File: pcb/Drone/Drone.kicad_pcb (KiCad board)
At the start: 2 copper layers, 72 x 72 mm, 61 parts, among them J1 USB_C_Receptacle_USB2.0_16P, J10 JST1.25, J2 JST1.25, J3 JST1.25, J4 JST1.25, J5 JST1.25, J6 JST1.25, J7 JST1.25, J8 JST1.25, J9 JST1.25, Q1 SS8050, Q2 SS8050, Q3 Si2301, SW1 RST, SW2 BOOT, U1 esp32s3_wroom1, U10 AP2112K-3.3, U2 DW01A, U4 USBLC6-2SC6, U5 8205, U6 CP2102, U8 ME6211C33M5, U9 ME6211C33M5

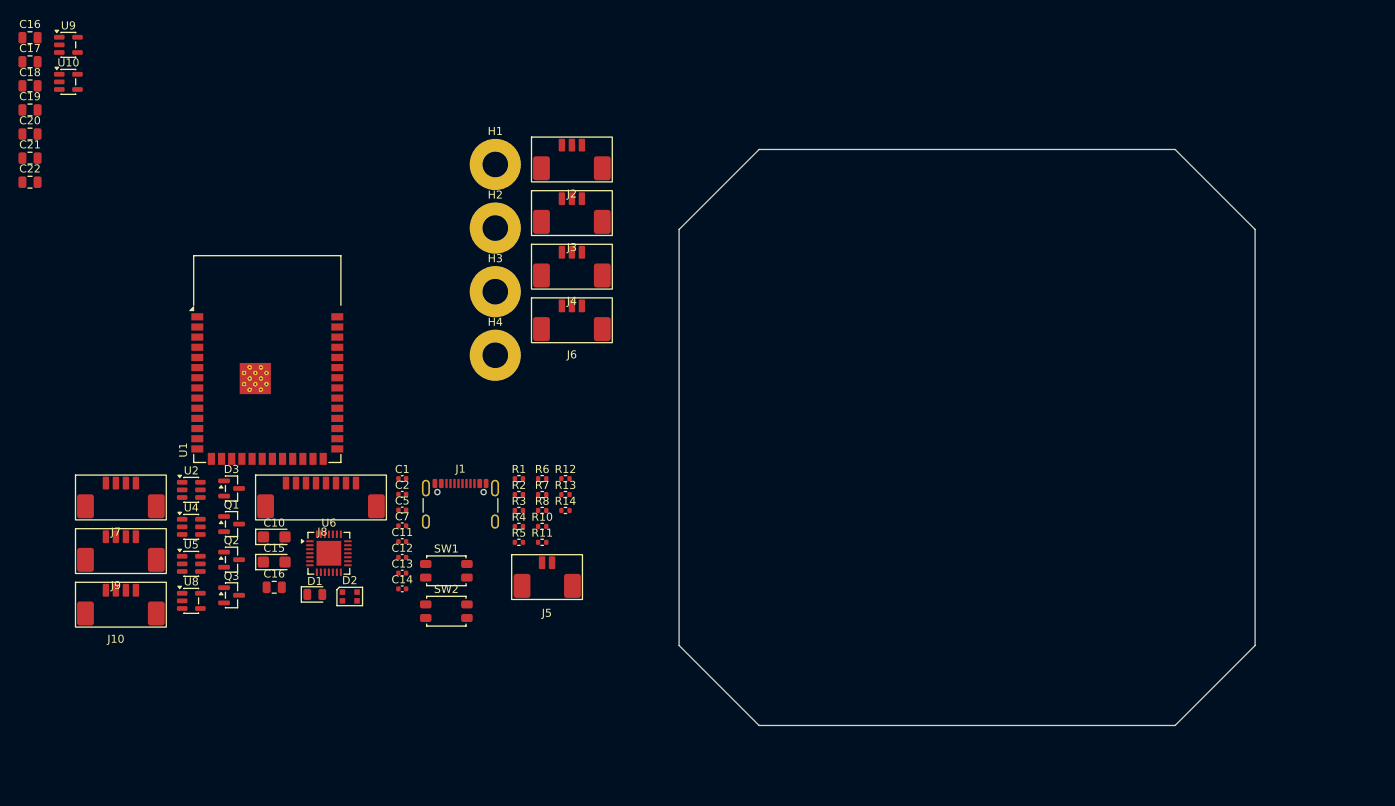
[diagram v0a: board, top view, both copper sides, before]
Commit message: pcb layout: complete component positions
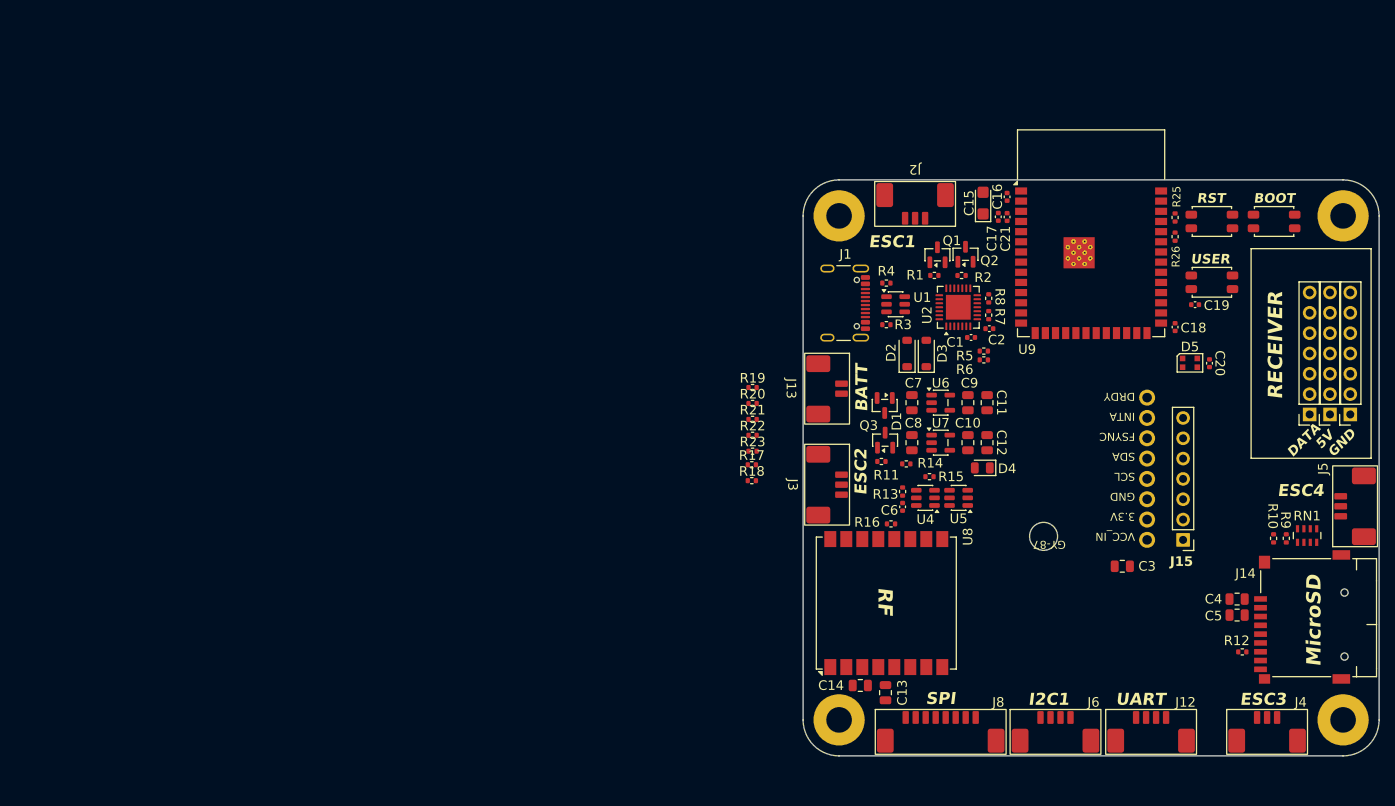
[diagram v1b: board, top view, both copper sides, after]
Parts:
- removed the C16 at (71.6, 113.2)
- removed the C16 at (41.1, 44.5)
- removed C22: 0.1u, Capacitor_SMD:C_0805_2012Metric
- removed J7: JST1.25, JST_1.25mm_RA_SMD:JST_1.25mm_RA_SMD_4P
- removed U10: AP2112K-3.3, Package_TO_SOT_SMD:SOT-23-5
- added C16: 0.1u, Capacitor_SMD:C_0402_1005Metric, F.Cu at (163.2, 64.4)
- added C3: 0.1u, Capacitor_SMD:C_0805_2012Metric, F.Cu at (177.6, 110.6)
- added C4: 10u, Capacitor_SMD:C_0805_2012Metric, F.Cu at (192.0, 114.7)
- added C6: 0.1u, Capacitor_SMD:C_0402_1005Metric, F.Cu at (150.1, 103.2)
- added C8: 22u, Capacitor_SMD:C_0805_2012Metric, F.Cu at (151.3, 95.2)
- added C9: 10u, Capacitor_SMD:C_0805_2012Metric, F.Cu at (158.3, 90.2)
- added D4: Red, LED_SMD:LED_0805_2012Metric, F.Cu at (160.1, 98.3)
- added D5: WS2812B-2020, LED_SMD:LED_WS2812B-2020_PLCC4_2.0x2.0mm, F.Cu at (186.1, 85.2)
- added J11: 2.54mm, Connector_PinSocket_2.54mm:PinSocket_1x07_P2.54mm_Vertical, F.Cu at (201.0, 91.6)
- added J12: JST1.25, Drone_local_footprints:JST_1.25mm_RA_SMD_4P, F.Cu at (179.3, 129.5)
- added J13: JST1.25, Drone_local_footprints:JST_1.25mm_RA_SMD_2P, F.Cu at (142.5, 87.8)
- added J14: Micro_SD_Card_Det1, Drone_local_footprints:Micro_SD_Card_Socket, F.Cu at (201.9, 117.9)
- added J15: JST1.25, Connector_PinHeader_2.54mm:PinHeader_1x07_P2.54mm_Vertical, F.Cu at (185.2, 107.3)
- added R15: 1K, Resistor_SMD:R_0402_1005Metric, F.Cu at (153.5, 99.4)
- added R16: 22R, Resistor_SMD:R_0402_1005Metric, F.Cu at (148.7, 105.3)
- added R17: 10K, Resistor_SMD:R_0402_1005Metric, F.Cu at (131.3, 97.9)
- added R18: 22R, Resistor_SMD:R_0402_1005Metric, F.Cu at (131.3, 99.9)
- added R19: 22R, Resistor_SMD:R_0402_1005Metric, F.Cu at (131.4, 88.3)
- added R20: 10K, Resistor_SMD:R_0402_1005Metric, F.Cu at (131.4, 90.2)
- added R21: 10K, Resistor_SMD:R_0402_1005Metric, F.Cu at (131.4, 92.2)
- added R22: 10K, Resistor_SMD:R_0402_1005Metric, F.Cu at (131.4, 94.2)
- added R23: 10K, Resistor_SMD:R_0402_1005Metric, F.Cu at (131.4, 96.2)
- added R25: 0R, Resistor_SMD:R_0402_1005Metric, F.Cu at (184.2, 67.0)
- added R26: 0R, Resistor_SMD:R_0402_1005Metric, F.Cu at (184.2, 69.4)
- added R9: 10K, Resistor_SMD:R_0402_1005Metric, F.Cu at (198.1, 107.1)
- added RN1: 10K, Resistor_SMD:R_Array_Concave_4x0603, F.Cu at (200.7, 106.8)
- added SW3: RST, Button_Switch_SMD:SW_SPST_EVQP2_MiddlePushTravel_H2.5mm, F.Cu at (188.8, 67.5)
- added U3: GY-87, Drone_local_footprints:GY-87, F.Cu at (180.7, 107.3)
- added U7: ME6211C33M5, Package_TO_SOT_SMD:SOT-23-5, F.Cu at (154.9, 95.2)
- C1: value 0.1u -> 1u
- C10: value 22u -> 10u; footprint Capacitor_Tantalum_SMD:CP_EIA-3216-10_Kemet-I -> Capacitor_SMD:C_0805_2012Metric
- C11: value 1u -> 0.1u; footprint Capacitor_SMD:C_0402_1005Metric -> Capacitor_SMD:C_0805_2012Metric
- C12, C14, C5: footprint Capacitor_SMD:C_0402_1005Metric -> Capacitor_SMD:C_0805_2012Metric
- C13: value 0.1u -> 22u; footprint Capacitor_SMD:C_0402_1005Metric -> Capacitor_SMD:C_0805_2012Metric
- C17, C20, C21: footprint Capacitor_SMD:C_0805_2012Metric -> Capacitor_SMD:C_0402_1005Metric
- C18: value 22u -> 0.1u; footprint Capacitor_SMD:C_0805_2012Metric -> Capacitor_SMD:C_0402_1005Metric
- C19: value 10u -> 0.1u; footprint Capacitor_SMD:C_0805_2012Metric -> Capacitor_SMD:C_0402_1005Metric
- C7: value 10u -> 22u; footprint Capacitor_SMD:C_0402_1005Metric -> Capacitor_SMD:C_0805_2012Metric
- D1: value Red -> BAT54C; footprint LED_SMD:LED_0805_2012Metric -> Package_TO_SOT_SMD:SOT-23
- D2: value WS2812B-2020 -> 1N5819; footprint LED_SMD:LED_WS2812B-2020_PLCC4_2.0x2.0mm -> Diode_SMD:D_SOD-123
- D3: value BAT54C -> 1N5819; footprint Package_TO_SOT_SMD:SOT-23 -> Diode_SMD:D_SOD-123
- J10, J9: value JST1.25 -> 2.54mm; footprint JST_1.25mm_RA_SMD:JST_1.25mm_RA_SMD_4P -> Connector_PinSocket_2.54mm:PinSocket_1x07_P2.54mm_Vertical
- J2, J3, J4: footprint JST_1.25mm_RA_SMD:JST_1.25mm_RA_SMD_3P -> Drone_local_footprints:JST_1.25mm_RA_SMD_3P
- J5: footprint JST_1.25mm_RA_SMD:JST_1.25mm_RA_SMD_2P -> Drone_local_footprints:JST_1.25mm_RA_SMD_3P
- J6: footprint JST_1.25mm_RA_SMD:JST_1.25mm_RA_SMD_3P -> Drone_local_footprints:JST_1.25mm_RA_SMD_4P
- J8: footprint JST_1.25mm_RA_SMD:JST_1.25mm_RA_SMD_8P -> Drone_local_footprints:JST_1.25mm_RA_SMD_8P
- R1: value 4K7 -> 10K
- R10: value 5K1 -> 10K
- R11: value 47K5 -> 10K
- R12: value 100 -> 22R
- R13: value 1K -> 100
- R14: value 10K -> 2K
- R3: value 10K -> 5K1
- R4: value 22K1 -> 5K1
- R5: value 5K1 -> 22K1
- R6: value 10K -> 47K5
- R7: value 10K -> 4K7
- R8: value 2K -> 10K
- SW1: value RST -> BOOT
- SW2: value BOOT -> USER
- U1: value esp32s3_wroom1 -> USBLC6-2SC6; footprint RF_Module:ESP32-S3-WROOM-1 -> Package_TO_SOT_SMD:SOT-23-6
- U2: value DW01A -> CP2102; footprint Package_TO_SOT_SMD:SOT-23-6 -> Package_DFN_QFN:QFN-28-1EP_5x5mm_P0.5mm_EP3.1x3.1mm
- U4: value USBLC6-2SC6 -> DW01A
- U6: value CP2102 -> AP2112K-3.3; footprint Package_DFN_QFN:QFN-28-1EP_5x5mm_P0.5mm_EP3.1x3.1mm -> Package_TO_SOT_SMD:SOT-23-5
- U8: value ME6211C33M5 -> Ai-Thinker-Ra-02; footprint Package_TO_SOT_SMD:SOT-23-5 -> RF_Module:Ai-Thinker-Ra-01-LoRa
- U9: value ME6211C33M5 -> esp32s3_wroom1; footprint Package_TO_SOT_SMD:SOT-23-5 -> RF_Module:ESP32-S3-WROOM-1
- moved J9 156.3 mm to (206.1, 91.6), turned to 180 degrees
- moved J10 154.6 mm to (203.6, 91.6), turned to 180 degrees
- moved C20 150.2 mm to (188.5, 85.2), turned to -90 degrees
- moved C19 147.7 mm to (186.7, 77.9)
- moved C18 146.3 mm to (184.2, 80.7), turned to -90 degrees
- moved U9 130.0 mm to (173.7, 69.0)
- moved C17 122.6 mm to (162.1, 66.9), turned to 90 degrees
- moved C21 122.4 mm to (163.2, 66.9), turned to -90 degrees
- moved H4 115.4 mm to (205.2, 129.8)
- moved SW1 112.3 mm to (196.6, 67.5)
- moved H3 106.4 mm to (205.2, 66.8)
- moved C5 105.2 mm to (192.0, 116.7), turned to 180 degrees
- moved J4 104.6 mm to (194.4, 129.5)
- moved SW2 104.2 mm to (188.8, 75.1)
- moved J5 100.0 mm to (204.9, 104.3), turned to 90 degrees
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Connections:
- C1 pad 1: /GPIO0 -> +3V3
- C10 pad 1: +3V3 -> +3V3_SENS
- C12 pad 1: Net-(U6-VBUS) -> +3V3_SENS
- C13 pad 1: Net-(U2-VCC) -> GND
- C13 pad 2: Net-(J5-Pin_2) -> +3V3
- C14 pad 1: RGB_POW -> +3V3
- C17 pad 1: +3V3 -> GND
- C17 pad 2: GND -> /CHIP_PU
- C18 pad 1: RGB_POW -> /GPIO0
- C19 pad 1: +3V3_SENS -> /USR_BUTTON
- C2 pad 1: /CHIP_PU -> Net-(U2-VBUS)
- C20 pad 1: +3V3_SENS -> +5V
- C21 pad 1: +3V3 -> /CHIP_PU
- C7 pad 1: GND -> +5V
- C7 pad 2: /CHIP_PU -> GND
- D1 pad 1: GND -> VBEC
- D1 pad 2: Net-(D1-A) -> VBUS
- D2 pad 1: unconnected-(D2-DOUT-Pad1) -> +5V
- D2 pad 2: GND -> VBUS
- D3 pad 1: VBEC -> +5V
- D3 pad 2: VBUS -> VBEC
- J10 pad 1: +3V3 -> unconnected-(J10-Pin_1-Pad1)
- J10 pad 2: GND -> unconnected-(J10-Pin_2-Pad2)
- J10 pad 3: /SCL1 -> unconnected-(J10-Pin_3-Pad3)
- J10 pad 4: /SDA1 -> unconnected-(J10-Pin_4-Pad4)
- J5 pad 1: +BATT -> GND
- J5 pad 2: Net-(J5-Pin_2) -> unconnected-(J5-Pin_2-Pad2)
- J6 pad 1: GND -> +3V3
- J6 pad 2: unconnected-(J6-Pin_2-Pad2) -> GND
- J6 pad 3: /PWM4 -> /SCL1
- J8 pad 4: /MISO -> /GPIO13
- J9 pad 1: +3V3 -> unconnected-(J9-Pin_1-Pad1)
- J9 pad 2: GND -> unconnected-(J9-Pin_2-Pad2)
- J9 pad 3: /TX -> unconnected-(J9-Pin_3-Pad3)
- J9 pad 4: /RX -> unconnected-(J9-Pin_4-Pad4)
- Q3 pad 2: RGB_POW -> +5V
- R1 pad 1: Net-(U6-~{RST}) -> /DTR
- R1 pad 2: +3V3 -> Net-(Q1-B)
- R10 pad 1: Net-(J1-CC1) -> +3V3
- R10 pad 2: GND -> /CS_uSD
- R11 pad 1: Net-(U6-VBUS) -> GND
- R11 pad 2: GND -> Net-(Q3-G)
- R12 pad 1: +BATT -> /GPIO13
- R12 pad 2: Net-(U2-VCC) -> Net-(J14-DAT0)
- R13 pad 1: Net-(U2-CS) -> +BATT
- R13 pad 2: GND -> Net-(U4-VCC)
- R14 pad 1: GND -> Net-(D4-A)
- R14 pad 2: Net-(Q3-G) -> +5V
- R2 pad 1: Net-(U6-~{SUSPEND}) -> /RTS
- R2 pad 2: GND -> Net-(Q2-B)
- R3 pad 1: +3V3 -> Net-(J1-CC2)
- R3 pad 2: /CHIP_PU -> GND
- R4 pad 1: VBUS -> Net-(J1-CC1)
- R4 pad 2: Net-(U6-VBUS) -> GND
- R5 pad 1: Net-(J1-CC2) -> VBUS
- R5 pad 2: GND -> Net-(U2-VBUS)
- R6 pad 1: /DTR -> Net-(U2-VBUS)
- R6 pad 2: Net-(Q1-B) -> GND
- R7 pad 1: /RTS -> Net-(U2-~{RST})
- R7 pad 2: Net-(Q2-B) -> +3V3
- R8 pad 1: Net-(D1-A) -> Net-(U2-~{SUSPEND})
- R8 pad 2: RGB_POW -> GND
- SW1 pad 2: /CHIP_PU -> /GPIO0
- SW2 pad 2: /GPIO0 -> /USR_BUTTON
- U1 pad 1: GND -> Net-(J1-D--PadA7)
- U1 pad 2: +3V3 -> GND
- U1 pad 3: /CHIP_PU -> Net-(J1-D+-PadA6)
- U1 pad 4: /GPIO4 -> /USB_D+
- U1 pad 5: /GPIO5 -> VBUS
- U1 pad 6: /GPIO6 -> /USB_D-
- U2 pad 1: Net-(U2-OD) -> unconnected-(U2-DCD-Pad1)
- U2 pad 2: Net-(U2-CS) -> unconnected-(U2-RI-Pad2)
- U2 pad 3: Net-(U2-OC) -> GND
- U2 pad 4: unconnected-(U2-TD-Pad4) -> /USB_D+
- U2 pad 5: Net-(U2-VCC) -> /USB_D-
- U2 pad 6: Net-(J5-Pin_2) -> +3V3
- U4 pad 1: Net-(J1-D--PadA7) -> Net-(U4-OD)
- U4 pad 2: GND -> Net-(U4-CS)
- U4 pad 3: Net-(J1-D+-PadA6) -> Net-(U4-OC)
- U4 pad 4: /USB_D+ -> unconnected-(U4-TD-Pad4)
- U4 pad 5: VBUS -> Net-(U4-VCC)
- U4 pad 6: /USB_D- -> Net-(J13-Pin_2)
- U5 pad 4: Net-(U2-OC) -> Net-(U4-OC)
- U5 pad 6: Net-(U2-OD) -> Net-(U4-OD)
- U6 pad 1: unconnected-(U6-DCD-Pad1) -> +5V
- U6 pad 2: unconnected-(U6-RI-Pad2) -> GND
- U6 pad 3: GND -> unconnected-(U6-EN-Pad3)
- U6 pad 4: /USB_D+ -> unconnected-(U6-NC-Pad4)
- U6 pad 5: /USB_D- -> +3V3
- U8 pad 1: RGB_POW -> GND
- U8 pad 3: unconnected-(U8-CE-Pad3) -> +3V3
- U8 pad 4: unconnected-(U8-NC-Pad4) -> /RF_RST
- U8 pad 5: +3V3 -> unconnected-(U8-DIO0-Pad5)
- U9 pad 1: RGB_POW -> GND
- U9 pad 2: GND -> +3V3
- U9 pad 3: unconnected-(U9-CE-Pad3) -> /CHIP_PU
- U9 pad 4: unconnected-(U9-NC-Pad4) -> /GPIO4
- U9 pad 5: +3V3_SENS -> /GPIO5
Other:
- outline, holes or cut-outs redrawn
- copper layers 2 -> 4
- board text added: "5V"
- board text added: "BATT"
- board text added: "BOOT"
- board text added: "DATA"
- board text added: "ESC1"
- board text added: "ESC2"
- board text added: "ESC3"
- board text added: "ESC4"
- board text added: "GND"
- board text added: "I2C1"
- board text added: "MicroSD"
- board text added: "RECEIVER"
- board text added: "RF"
- board text added: "RST"
- board text added: "SPI"
- board text added: "UART"
- board text added: "USER"

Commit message: fc pcb: done; 3d model: initial frame and physical properties
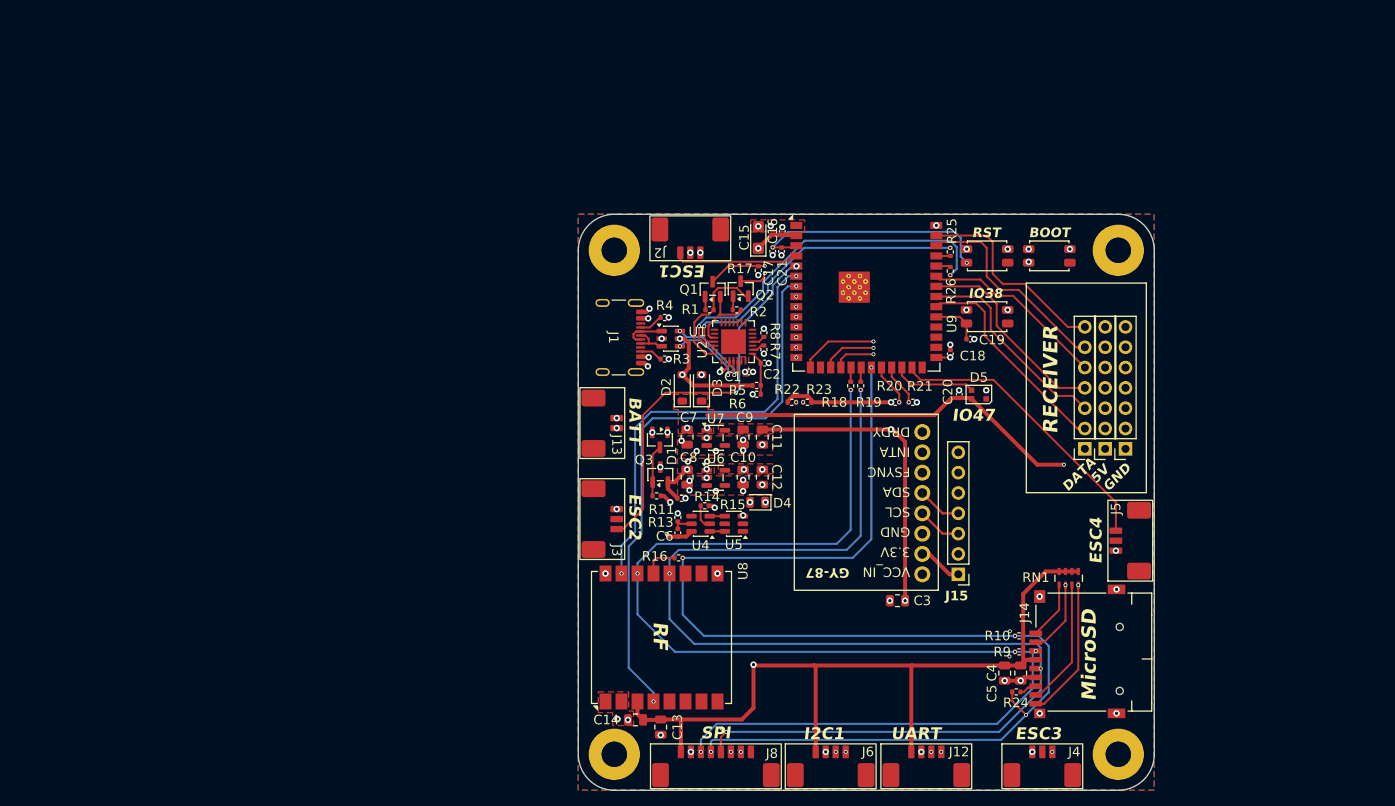
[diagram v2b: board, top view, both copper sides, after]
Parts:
- removed R12: 22R, Resistor_SMD:R_0402_1005Metric
- added R24: 22R, Resistor_SMD:R_0402_1005Metric, F.Cu at (164.4, 126.3)
- J12, J6: footprint Drone_local_footprints:JST_1.25mm_RA_SMD_4P -> Local Footprints:JST_1.25mm_RA_SMD_4P
- J13: footprint Drone_local_footprints:JST_1.25mm_RA_SMD_2P -> Local Footprints:JST_1.25mm_RA_SMD_2P
- J14: footprint Drone_local_footprints:Micro_SD_Card_Socket -> Local Footprints:Micro_SD_Card_Socket
- J2, J3, J4, J5: footprint Drone_local_footprints:JST_1.25mm_RA_SMD_3P -> Local Footprints:JST_1.25mm_RA_SMD_3P
- J8: footprint Drone_local_footprints:JST_1.25mm_RA_SMD_8P -> Local Footprints:JST_1.25mm_RA_SMD_8P
- U3: footprint Drone_local_footprints:GY-87 -> Local Footprints:GY-87
- moved R9 36.3 mm to (164.7, 121.3), turned to 180 degrees
- moved R10 34.1 mm to (164.7, 119.3), turned to 180 degrees
- moved C20 31.5 mm to (157.2, 89.1), turned to 90 degrees
- moved C4 30.5 mm to (162.9, 124.0), turned to -90 degrees
- moved RN1 30.3 mm to (170.9, 112.1)
- moved U6 29.6 mm to (126.8, 99.5)
- moved R5 28.7 mm to (131.9, 88.0)
- moved R6 28.7 mm to (131.9, 89.1)
- moved C17 28.5 mm to (133.9, 71.2)
- moved C21 28.5 mm to (135.0, 71.2)
- moved C10 28.4 mm to (130.2, 99.5)
- moved C9 28.4 mm to (130.2, 94.5)
- moved SW2 28.4 mm to (160.7, 79.4)
- moved SW3 28.4 mm to (160.7, 71.8)
- moved J8 28.4 mm to (122.4, 133.8)
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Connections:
- net /GPIO11 renamed Net-(U9-IO11)
- net /GPIO12 renamed Net-(U9-IO12)
- C10 pad 1: +3V3_SENS -> +3V3
- C11 pad 1: +3V3 -> +3V3_SENS
- C12 pad 1: +3V3_SENS -> +3V3
- C9 pad 1: +3V3 -> +3V3_SENS
- J10 pad 1: unconnected-(J10-Pin_1-Pad1) -> +5V
- J10 pad 2: unconnected-(J10-Pin_2-Pad2) -> +5V
- J10 pad 3: unconnected-(J10-Pin_3-Pad3) -> +5V
- J10 pad 4: unconnected-(J10-Pin_4-Pad4) -> +5V
- J10 pad 5: unconnected-(J10-Pin_5-Pad5) -> +5V
- J10 pad 6: unconnected-(J10-Pin_6-Pad6) -> +5V
- J11 pad 2: /PWM6 -> /RX_PWM6
- J11 pad 3: /PWM5 -> /RX_PWM5
- J11 pad 4: /PWM4 -> /RX_PWM4
- J11 pad 5: /PWM3 -> /RX_PWM3
- J11 pad 6: /PWM2 -> /RX_PWM2
- J11 pad 7: /PPM/PWM1 -> /RX_PWM1
- J14 pad 9: /CARD_DETECT -> /CARD_DET
- J15 pad 1: +3V3 -> +3V3_SENS
- J2 pad 3: /PWM1 -> /ESC_PWM1
- J3 pad 3: /PWM2 -> /ESC_PWM2
- J4 pad 3: /PWM3 -> /ESC_PWM3
- J5 pad 3: /PWM4 -> /ESC_PWM4
- J8 pad 4: /GPIO13 -> /MISO
- J8 pad 6: /CS -> /CS_PERIP
- J8 pad 7: /GPIOx -> /GPIO16
- J9 pad 1: unconnected-(J9-Pin_1-Pad1) -> GND
- J9 pad 2: unconnected-(J9-Pin_2-Pad2) -> GND
- J9 pad 3: unconnected-(J9-Pin_3-Pad3) -> GND
- J9 pad 4: unconnected-(J9-Pin_4-Pad4) -> GND
- J9 pad 5: unconnected-(J9-Pin_5-Pad5) -> GND
- J9 pad 6: unconnected-(J9-Pin_6-Pad6) -> GND
- R10 pad 2: /CS_uSD -> /MISO
- R16 pad 1: /GPIO13 -> /MISO
- R9 pad 2: Net-(J14-DAT2) -> /MOSI
- RN1 pad 1: /CARD_DETECT -> Net-(J14-DAT2)
- RN1 pad 2: Net-(J14-DAT1) -> /CS_uSD
- RN1 pad 3: /GPIO13 -> Net-(J14-DAT1)
- RN1 pad 4: /MOSI -> /CARD_DET
- U9 pad 10: /GPIO17 -> /ESC_PWM3
- U9 pad 11: /GPIO18 -> /RX
- U9 pad 12: /GPIO8 -> /TX
- U9 pad 13: /GPIO19 -> /SDA1
- U9 pad 14: /GPIO20 -> /SCL1
- U9 pad 15: /GPIO3 -> /CARD_DET
- U9 pad 17: /GPIO9 -> /CS_uSD
- U9 pad 18: /GPIO10 -> /DRDY
- U9 pad 21: /GPIO13 -> /MISO
- U9 pad 22: /GPIO14 -> /SCL0
- U9 pad 23: /GPIO21 -> /SDA0
- U9 pad 24: /GPIO47 -> /RGB
- U9 pad 25: /GPIO48 -> /ESC_PWM4
- U9 pad 31: /GPIO38 -> /USR_BUTTON
- U9 pad 32: /GPIO39 -> /RX_PWM6
- U9 pad 33: /GPIO40 -> /RX_PWM5
- U9 pad 34: /GPIO41 -> /RX_PWM4
- U9 pad 35: /GPIO42 -> /RX_PWM3
- U9 pad 38: /GPIO2 -> /RX_PWM2
- U9 pad 39: /GPIO1 -> /RX_PWM1
- U9 pad 4: /GPIO4 -> /ESC_PWM1
- U9 pad 5: /GPIO5 -> /ESC_PWM2
- U9 pad 6: /GPIO6 -> /CS_RF
- U9 pad 7: /GPIO7 -> /RF_RST
- U9 pad 8: /GPIO15 -> /CS_PERIP
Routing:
- net +3V3: track 0.00 -> 163.6 mm, vias 0 -> 7
- net /MISO: track 0.00 -> 155.9 mm, vias 0 -> 5
- net /MOSI: track 0.00 -> 154.3 mm, vias 0 -> 5
- net /SCK: track 0.00 -> 148.3 mm, vias 0 -> 4
- net /ESC_PWM3: track 0.00 -> 78.4 mm, vias 0 -> 2
- net /CARD_DET: track 0.00 -> 76.4 mm, vias 0 -> 2
- net +5V: track 0.00 -> 75.9 mm, vias 0 -> 7
- net +3V3_SENS: track 0.00 -> 71.7 mm, vias 0 -> 4
- net /RF_RST: track 0.00 -> 70.7 mm, vias 0 -> 2
- net /RX: track 0.00 -> 63.5 mm, vias 0 -> 2
- net /CS_uSD: track 0.00 -> 63.4 mm, vias 0 -> 2
- net /TX: track 0.00 -> 61.8 mm, vias 0 -> 2
- net /CS_PERIP: track 0.00 -> 60.3 mm, vias 0 -> 2
- net /GPIO0: track 0.00 -> 59.1 mm, vias 0 -> 3
- net /GPIO16: track 0.00 -> 58.7 mm, vias 0 -> 2
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- added copper zone on F.Cu, net +3V3
- added copper zone on In1.Cu, net +3V3
- added copper zone on F.Cu, net +3V3_SENS
- added copper zone on F.Cu, net +5V
- added copper zone on In1.Cu, net +5V
- added copper zone on B.Cu, net GND
- added copper zone on F.Cu, net GND
- added copper zone on In1.Cu, net GND
- added copper zone on In2.Cu, net GND
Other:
- board text added: "IO38"
- board text added: "IO47"
- board text removed: "USER"

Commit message: development: 3d, power board, fc
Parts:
- added G***: LOGO, Local Footprints:logo1, F.Cu at (137.3, 122.1)
- C11, C12, C14, C3, C5: footprint Capacitor_SMD:C_0805_2012Metric -> Capacitor_SMD:C_0402_1005Metric
- J10, J11, J9: footprint Connector_PinSocket_2.54mm:PinSocket_1x07_P2.54mm_Vertical -> Local Footprints:_PinSocket_1x07_P2.54mm_Vertical
- moved C11 0.65 mm to (132.0, 94.2)
- moved C12 0.65 mm to (132.0, 99.2)
- moved C3 0.50 mm to (150.0, 114.9)
- moved C5 0.47 mm to (164.9, 123.5)
- moved C14 0.45 mm to (116.3, 129.8)
- moved J12 0.20 mm to (151.2, 133.6)
- moved J4 0.20 mm to (166.4, 133.6)
- moved J5 0.20 mm to (176.6, 108.7)
- moved J6 0.20 mm to (139.3, 133.6)
- moved J8 0.20 mm to (122.4, 133.6)
- moved J13 0.20 mm to (114.6, 92.1)
- moved J3 0.20 mm to (114.6, 103.5)
- moved J2 0.20 mm to (124.9, 71.6)
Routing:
- net +3V3: track 163.6 -> 161.9 mm, vias 7 -> 6
- net /ESC_PWM1: track 15.7 -> 16.7 mm
- net +3V3_SENS: track 71.7 -> 72.5 mm
- net GND: track 12.3 -> 12.9 mm
- removed copper zone on In1.Cu, net +3V3
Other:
- board text added: "Metrology Lab"
- board text added: "OISP Drone"
